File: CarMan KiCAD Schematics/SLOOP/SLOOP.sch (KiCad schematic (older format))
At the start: 27 parts

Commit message: updated Epal and Sloop
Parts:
- removed BTN?: MRESET, Lafayette_Electric_Car_Footprints:PushButton, symbol Lafayette_Electric_Car_Internals:PushButton
- removed BTN?: GLVMS, Lafayette_Electric_Car_Footprints:PushButton, symbol Lafayette_Electric_Car_Internals:PushButton
- removed BTN?: RBRB, Lafayette_Electric_Car_Footprints:PushButton, symbol Lafayette_Electric_Car_Internals:PushButton
- removed BTN?: LBRB, Lafayette_Electric_Car_Footprints:PushButton, symbol Lafayette_Electric_Car_Internals:PushButton
- removed BTN?: CPRESET, Lafayette_Electric_Car_Footprints:PushButton, symbol Lafayette_Electric_Car_Internals:PushButton
- removed U?: MRESET RELAY, symbol Lafayette_Electric_Car_Internals:NO_Relay
- removed U?: CPBRB, symbol Lafayette_Electric_Car_Internals:SWITCH
- removed U?: CPRELAY, symbol Lafayette_Electric_Car_Internals:NO_Relay
- removed U?: DISCHARGE RELAY, symbol Lafayette_Electric_Car_Internals:NO_Relay
- removed U? (x4): NO_Relay, symbol Lafayette_Electric_Car_Internals:NO_Relay
- added BTN?: GLVMS, Lafayette_Electric_Car_Footprints:PushButton, symbol Lafayette_Electric_Car_Internals:NC_PushButton
- added BTN?: RBRB, Lafayette_Electric_Car_Footprints:PushButton, symbol Lafayette_Electric_Car_Internals:NC_PushButton
- added BTN?: LBRB, Lafayette_Electric_Car_Footprints:PushButton, symbol Lafayette_Electric_Car_Internals:NC_PushButton
- added BTN?: CPBRB, Lafayette_Electric_Car_Footprints:PushButton, symbol Lafayette_Electric_Car_Internals:NC_PushButton
- added BTN?: MRESET, Lafayette_Electric_Car_Footprints:PushButton, symbol Lafayette_Electric_Car_Internals:PushButton
- added BTN?: CPRESET, Lafayette_Electric_Car_Footprints:PushButton, symbol Lafayette_Electric_Car_Internals:PushButton
- added CB? (x2): 5A Circuit Breaker, symbol Device:CircuitBreaker_1P
- added D?: FAULT LED, symbol Device:LED
- added L? (x5): L, symbol Device:L
- added U?: MRESET RELAY, symbol Lafayette_Electric_Car_Internals:NO_Relay
- added U?: CPRELAY, symbol Lafayette_Electric_Car_Internals:NO_Relay
- U?: value PACK1 AMS -> LPACK AMS
- U?: value PACK2 AMS -> RPACK AMS
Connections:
- net labels added: Earth
- wire segments 94 -> 64
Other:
- note added: "CARMAN\nENCLOSURE"
- note added: "COCKPIT"
- note added: "COOLING"
- note added: "Chassis Ground"
- note added: "DISCHARGE RELAY\n COIL"
- note added: "LEFT SIDE\n PANEL"
- note added: "LEFT\nAIRS\nCOILS"
- note added: "LEFT\nPACK"
- note added: "PEDALS"
- note added: "PFET\nINVERTER"
- note added: "RIGHT SIDE\n PANEL"
- note added: "RIGHT\nAIRS\nCOILS"
- note added: "RIGHT\nPACK"
- note added: "SUBSYSTEMS"
- note added: "W1"
- note added: "W13"
- note added: "W16"
- note added: "W2"
- note added: "W20"
- note added: "W21"
- note added: "W27"
- note removed: "AIRS\n"

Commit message: updated Sloop once more
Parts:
- removed BTN?: GLVMS, Lafayette_Electric_Car_Footprints:PushButton, symbol Lafayette_Electric_Car_Internals:NC_PushButton
- removed MES?: Voltmeter_DC, symbol Device:Voltmeter_DC
- removed MES?: Amperemeter_DC, symbol Device:Amperemeter_DC
- removed U?: BRAKE OVERTRAVEL, symbol Lafayette_Electric_Car_Internals:SWITCH
- added U?: GLVMS, symbol Lafayette_Electric_Car_Internals:SWITCH
- added U?: BOT SWITCH, symbol Lafayette_Electric_Car_Internals:NC_SWITCH
- D?: value FAULT LED -> GENERAL FAULT LED
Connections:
- wire segments 64 -> 61
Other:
- note added: "DASHBOARD"
- note added: "LOGIC\nINVERTER"
- note added: "Note 1:\nSUBSYSTEMS contains: SCADA Computer,\nTSI, CAN Bus, Dashboard Display,\nStatus Lights including: AMD and IMS Faults,\nI2C Line, PacMan Boards, Brake Light, IMD, \nand Sensors including: Temperature and\nFlow Rate Sensors"
- note added: "SUBSYSTEMS\n(See Note 1)"
- note added: "Voltmeter\nAmmeter"
- note added: "W22"
- note removed: "PFET\nINVERTER"
- note removed: "SUBSYSTEMS"
- note removed: "Voltmeter/Ammeter"

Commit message: Sloop Latching Logique
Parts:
- removed U?: IMD RELAY, symbol Lafayette_Electric_Car_Internals:SWITCH
- removed U?: LPACK AMS, symbol Lafayette_Electric_Car_Internals:SWITCH
- removed U?: RPACK AMS, symbol Lafayette_Electric_Car_Internals:SWITCH
- added BTN?: IMD RESET, Lafayette_Electric_Car_Footprints:PushButton, symbol Lafayette_Electric_Car_Internals:PushButton
- added BTN?: R_AMS RESET, Lafayette_Electric_Car_Footprints:PushButton, symbol Lafayette_Electric_Car_Internals:PushButton
- added BTN?: L_AMS_RESET, Lafayette_Electric_Car_Footprints:PushButton, symbol Lafayette_Electric_Car_Internals:PushButton
- added U?: IMD RELAY, symbol Lafayette_Electric_Car_Internals:NO_Relay2
- added U?: R_AMS RELAY, symbol Lafayette_Electric_Car_Internals:NO_Relay2
- added U?: L_AMS RELAY, symbol Lafayette_Electric_Car_Internals:NO_Relay2
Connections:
- wire segments 61 -> 95
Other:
- note added: "IMD\nLOW=FAULT"
- note added: "L_PACMAN\nLOW=FAULT"
- note added: "Note 2:\n wires denote \n\n wires denote a return path to the\n negative terminal of the GLV Battery"
- note added: "R_PACMAN\nLOW=FAULT"
- note added: "W24"

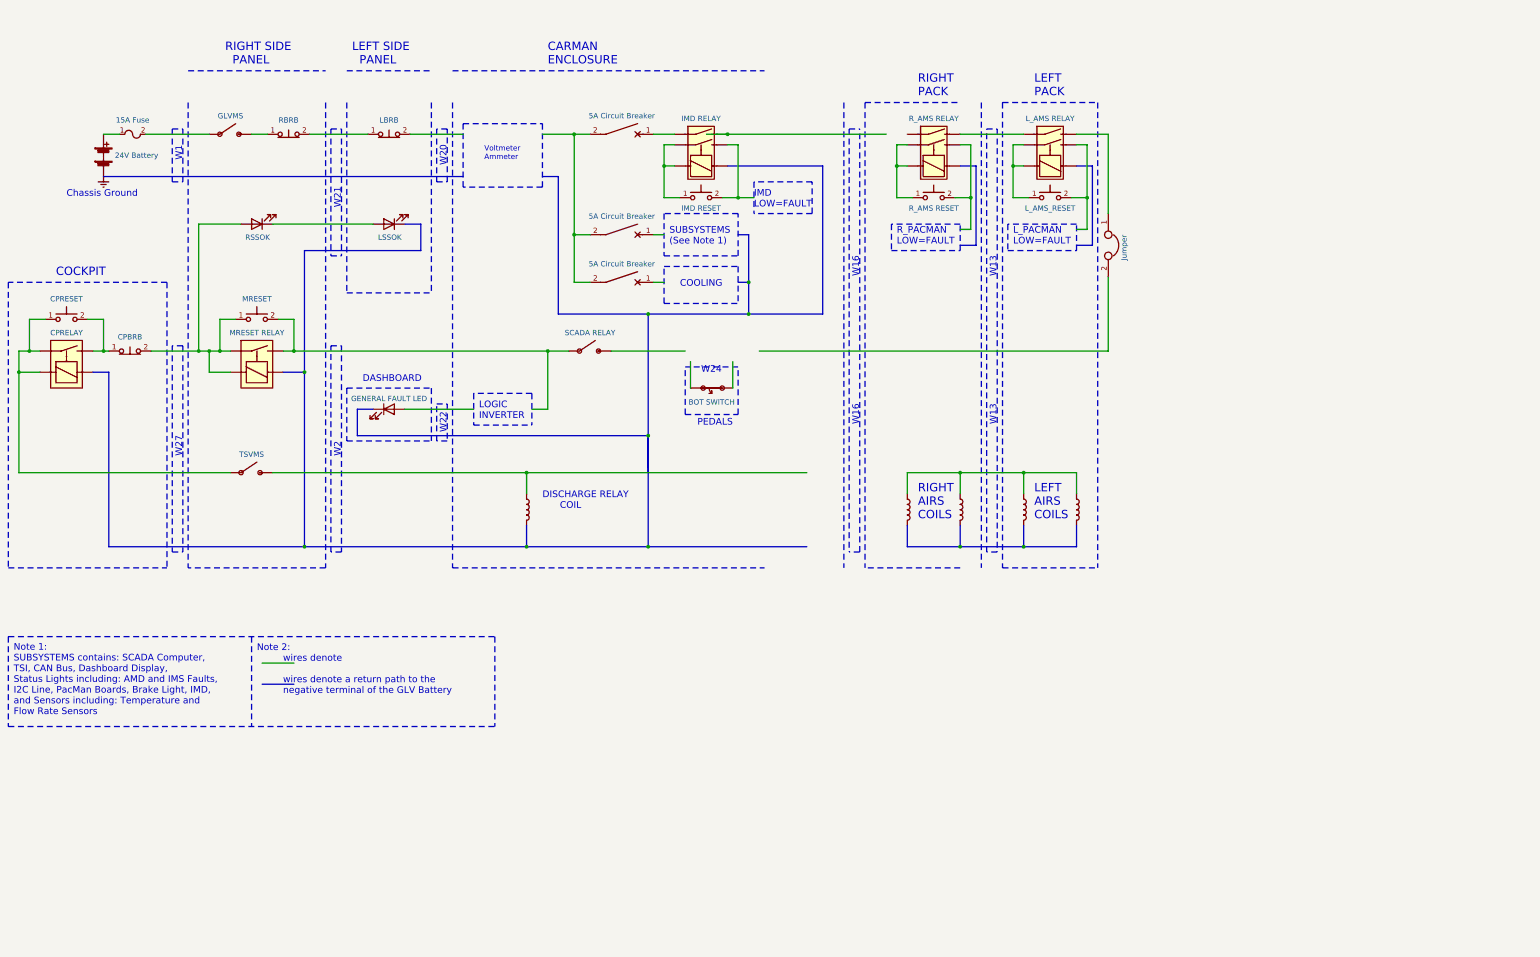
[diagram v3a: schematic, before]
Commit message: Added BOT brake light breaking
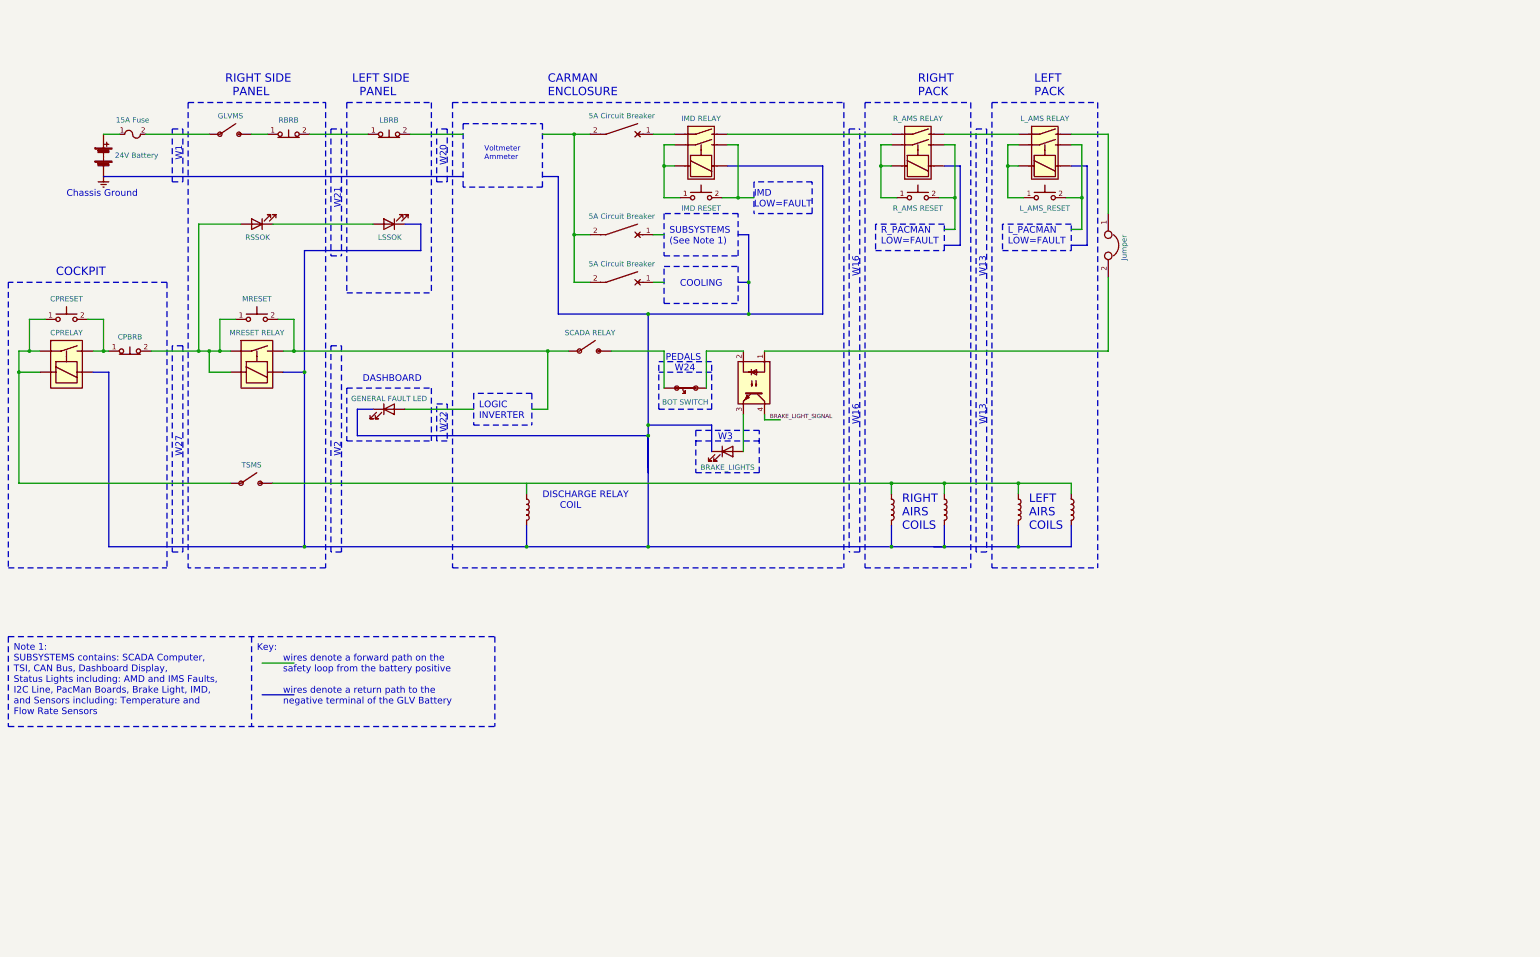
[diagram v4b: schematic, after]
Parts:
- added D?: BRAKE_LIGHTS, symbol Device:LED
- added U?: TLP293, Package_SO:SOIC-4_4.55x2.6mm_P1.27mm, symbol CarMan_KiCAD_Library:TLP293
- U?: value TSVMS -> TSMS
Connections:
- net labels added: BRAKE_LIGHT_SIGNAL
- wire segments 95 -> 97
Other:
- note added: "Key:\n wires denote a forward path on the\n safety loop from the battery positive\n\n wires denote a return path to the\n negative terminal of the GLV Battery"
- note added: "W3"
- note removed: "Note 2:\n wires denote \n\n wires denote a return path to the\n negative terminal of the GLV Battery"

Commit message: Updated latching logic
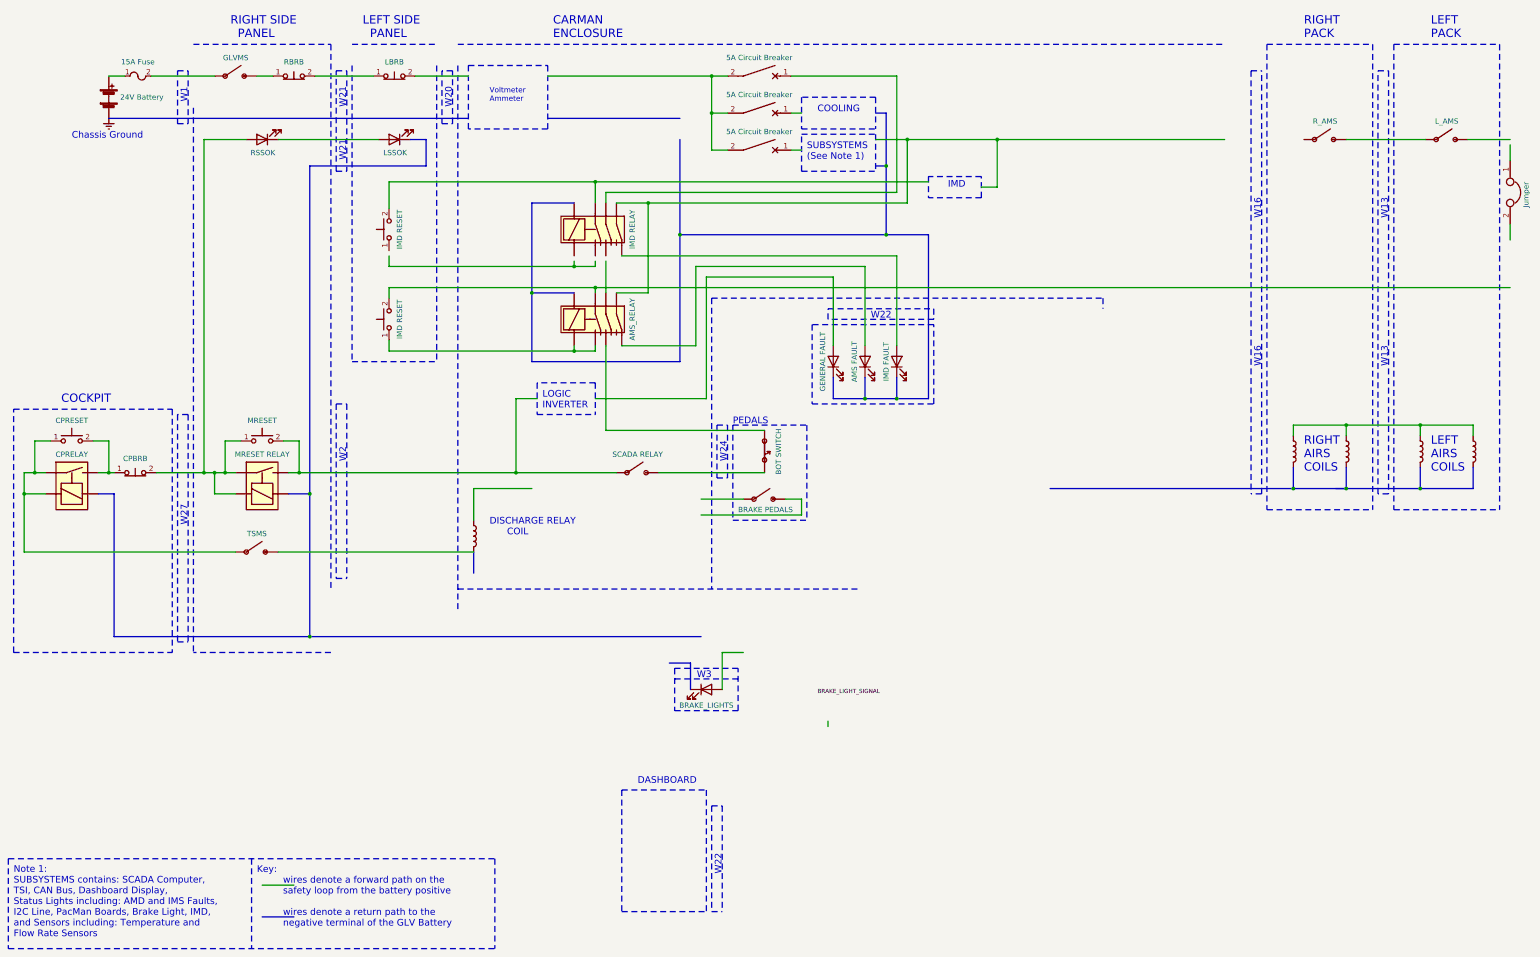
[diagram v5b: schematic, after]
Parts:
- removed BTN?: IMD RESET, Lafayette_Electric_Car_Footprints:PushButton, symbol Lafayette_Electric_Car_Internals:PushButton
- removed BTN?: R_AMS RESET, Lafayette_Electric_Car_Footprints:PushButton, symbol Lafayette_Electric_Car_Internals:PushButton
- removed BTN?: L_AMS_RESET, Lafayette_Electric_Car_Footprints:PushButton, symbol Lafayette_Electric_Car_Internals:PushButton
- removed CB?: 5A Circuit Breaker, symbol Device:CircuitBreaker_1P
- removed D?: GENERAL FAULT LED, symbol Device:LED
- removed U?: TLP293, Package_SO:SOIC-4_4.55x2.6mm_P1.27mm, symbol CarMan_KiCAD_Library:TLP293
- removed U?: IMD RELAY, symbol Lafayette_Electric_Car_Internals:NO_Relay2
- removed U?: R_AMS RELAY, symbol Lafayette_Electric_Car_Internals:NO_Relay2
- removed U?: L_AMS RELAY, symbol Lafayette_Electric_Car_Internals:NO_Relay2
- added BTN? (x2): IMD RESET, Lafayette_Electric_Car_Footprints:PushButton, symbol Lafayette_Electric_Car_Internals:PushButton
- added CB?: 5A Circuit Breaker, symbol Device:CircuitBreaker_1P
- added D?: IMD FAULT, symbol Device:LED
- added D?: AMS FAULT, symbol Device:LED
- added D?: GENERAL FAULT, symbol Device:LED
- added U?: BRAKE PEDALS, symbol Lafayette_Electric_Car_Internals:SWITCH
- added U?: R_AMS, symbol Lafayette_Electric_Car_Internals:SWITCH
- added U?: L_AMS, symbol Lafayette_Electric_Car_Internals:SWITCH
- added U?: IMD RELAY, symbol Lafayette_Electric_Car_Internals:NO_Relay3
- added U?: AMS_RELAY, symbol Lafayette_Electric_Car_Internals:NO_Relay3
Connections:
- wire segments 97 -> 111
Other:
- note added: "IMD"
- note removed: "IMD\nLOW=FAULT"
- note removed: "L_PACMAN\nLOW=FAULT"
- note removed: "R_PACMAN\nLOW=FAULT"

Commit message: updated Sloop once again
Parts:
- removed D?: IMD FAULT, symbol Device:LED
- removed D?: AMS FAULT, symbol Device:LED
- removed D?: GENERAL FAULT, symbol Device:LED
- added D?: GENERAL FAULT, symbol Device:LED
- added D?: AMS FAULT, symbol Device:LED
- added D?: IMD FAULT, symbol Device:LED
- BTN?: value IMD RESET -> AMS RESET
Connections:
- net labels removed: BRAKE_LIGHT_SIGNAL
- wire segments 111 -> 109
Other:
- note added: "BRAKE LIGHT"
- note added: "W26"

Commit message: updated Sloop once more
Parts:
- added U?: GLVMS, symbol Lafayette_Electric_Car_Internals:SWITCH
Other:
- note added: "Note 1:\nSUBSYSTEMS contains: SCADA Computer,\nTSI, CAN Bus, Dashboard Display,\nI2C Line, PacMan Boards, Brake Light, IMD, \nand Sensors including: Temperature and\nFlow Rate Sensors"
- note removed: "Note 1:\nSUBSYSTEMS contains: SCADA Computer,\nTSI, CAN Bus, Dashboard Display,\nStatus Lights including: AMD and IMS Faults,\nI2C Line, PacMan Boards, Brake Light, IMD, \nand Sensors including: Temperature and\nFlow Rate Sensors"
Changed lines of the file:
@@
 	1    0    0    -1
 $EndComp
-Wire Wire Line
-	1800 1300 1950 1300
 $Comp
 L Lafayette_Electric_Car_Internals:Fuse F?
@@
 $EndComp
 Wire Wire Line
-	3750 1300 4300 1300
-Wire Wire Line
 	3400 1900 4350 1900
 Text Notes 4200 950  0    79   ~ 0
@@
 Wire Bus Line
 	5200 1700 1800 1700
-Wire Wire Line
-	4700 1300 5200 1300
-Text Notes 900  7850 0    63   ~ 0
-Note 1:\nSUBSYSTEMS contains: SCADA Computer,\nTSI, CAN Bus, Dashboard Display,\nStatus Lights including: AMD and IMS Faults,\nI2C Line, PacMan Boards, Brake Light, IMD, \nand Sensors including: Temperature and\nFlow Rate Sensors
+Text Notes 900  7750 0    63   ~ 0
+Note 1:\nSUBSYSTEMS contains: SCADA Computer,\nTSI, CAN Bus, Dashboard Display,\nI2C Line, PacMan Boards, Brake Light, IMD, \nand Sensors including: Temperature and\nFlow Rate Sensors
 Wire Notes Line
 	5950 1200 5950 1800
 Wire Notes Line
 	5200 1800 5200 1200
-Wire Wire Line
-	2200 1300 2800 1300
-Wire Wire Line
-	3200 1300 3350 1300
 $Comp
 L Lafayette_Electric_Car_Internals:SWITCH U?
@@
 	0    1    1    0
 $EndComp
-Connection ~ 7500 1300
-Wire Wire Line
-	7500 1300 7650 1300
 Wire Notes Line
 	9050 1850 9050 2200
@@
 Text Notes 8400 2100 0    63   ~ 0
 SUBSYSTEMS\n(See Note 1)
-Text Notes 9900 2363 2    63   ~ 0
+Text Notes 9900 2150 2    63   ~ 0
 IMD
 Wire Notes Line
-	10050 2450 10050 2250
-Wire Notes Line
-	10050 2450 9550 2450
-Wire Notes Line
-	10050 2250 9550 2250
+	10050 2400 9550 2400
 Text Notes 8500 1650 0    63   ~ 0
 COOLING
@@
 Wire Bus Line
 	9150 1650 9150 2150
-Wire Wire Line
-	8250 1300 9250 1300
 Connection ~ 9150 2150
 Wire Wire Line
@@
 	0    1    1    0
 $EndComp
-Wire Notes Line
-	9550 2250 9550 2450
-Wire Wire Line
-	10050 2350 10200 2350
 Wire Bus Line
 	5950 1700 7200 1700
-Wire Wire Line
-	5950 1300 7500 1300
 Wire Bus Line
 	5800 4000 7200 4000
@@
 	9050 1900 9350 1900
 Wire Wire Line
-	6500 2400 6500 2500
-Wire Wire Line
-	9250 1300 9250 2400
-Wire Wire Line
-	6500 2400 9250 2400
-Wire Wire Line
 	6400 2300 6400 2500
 Wire Wire Line
-	10200 1900 10200 2350
+	10200 1900 10200 2300
 Connection ~ 9350 1900
 Wire Wire Line
@@
 Wire Wire Line
 	4450 2300 6400 2300
-Connection ~ 6400 2300
-Wire Wire Line
-	6400 2300 9550 2300
 Wire Wire Line
 	9350 2500 9350 1900
@@
 	9150 2150 9150 2800
 Wire Wire Line
-	6500 3850 6500 4650
-Wire Wire Line
 	5850 4350 5650 4350
 Wire Wire Line
 	5650 4350 5650 5050
-Wire Wire Line
-	5650 5050 6600 5050
-Wire Wire Line
-	6500 4650 8000 4650
-Wire Wire Line
-	7000 5050 8000 5050
-Wire Wire Line
-	5650 5050 3600 5050
-Connection ~ 5650 5050
-Connection ~ 3600 5050
 Wire Wire Line
 	2700 1900 2700 5050
@@
 Wire Wire Line
 	6400 3000 6400 3100
-Wire Wire Line
-	6500 3000 6500 3350
 Wire Notes Line
 	7650 5500 7550 5500
@@
 Wire Notes Line
 	7650 5200 7650 5500
+Connection ~ 6400 2300
+$Comp
+L Lafayette_Electric_Car_Internals:SWITCH U?
+U 1 1 5FCF618A
+P 9850 2150
+F 0 "U?" H 9800 2265 50  0001 C CNN
+F 1 "GLVMS" H 9800 2173 50  0001 C CNN
+F 2 "" H 9800 2350 50  0001 C CNN
+F 3 "" H 9800 2350 50  0001 C CNN
+	1    9850 2150
+	1    0    0    -1
+$EndComp
+Wire Notes Line
+	10050 2150 10050 2400
+Wire Notes Line
+	9550 2150 9550 2400
+Wire Notes Line
+	9550 2150 10050 2150
+Wire Wire Line
+	10000 2300 10200 2300
+Wire Wire Line
+	6400 2300 9600 2300
+Connection ~ 3600 5050
+Wire Wire Line
+	5650 5050 3600 5050
+Connection ~ 5650 5050
+Wire Wire Line
+	5650 5050 6600 5050
+Wire Wire Line
+	7000 5050 8000 5050
+Wire Wire Line
+	6500 4650 8000 4650
+Wire Wire Line
+	6500 3850 6500 4650
+Wire Wire Line
+	6500 3000 6500 3350
+Wire Wire Line
+	6500 2400 6500 2500
+Wire Wire Line
+	6500 2400 9250 2400
+Wire Wire Line
+	9250 1300 9250 2400
+Wire Wire Line
+	8250 1300 9250 1300
+Wire Wire Line
+	7500 1300 7650 1300
+Connection ~ 7500 1300
+Wire Wire Line
+	5950 1300 7500 1300
+Wire Wire Line
+	4700 1300 5200 1300
+Wire Wire Line
+	3750 1300 4300 1300
+Wire Wire Line
+	3200 1300 3350 1300
+Wire Wire Line
+	2200 1300 2800 1300
+Wire Wire Line
+	1800 1300 1950 1300
 $EndSCHEMATC
